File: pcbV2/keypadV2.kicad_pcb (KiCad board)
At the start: 2 copper layers, 93.7 x 93.3 mm, 79 parts, among them J1 Conn_01x02_Female, J2 USB_C_Receptacle, J3 Conn_01x03_Male, Q1 Q_NMOS_GSD, SW1 SW_Push, SW10 SW_Push, SW11 SW_Push, SW12 SW_Push, SW13 SW_SPDT, SW14 SW_Push, SW15 SW_Push, SW16 SW_Push, SW17 SW_DIP_x03, SW2 SW_Push, SW3 SW_Push, SW4 SW_Push, SW5 SW_Push, SW6 SW_Push, SW7 SW_Push, SW8 SW_Push, SW9 SW_Push, U1 Teensy4.0, U2 Waveshare_OLED_RGB

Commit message: component layout v1
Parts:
- added J6: Conn_01x03_Male, Connector_PinSocket_2.54mm:PinSocket_1x03_P2.54mm_Vertical, B.Cu at (160.8, 119.1)
- C13, C14, C15, D13, D26, D27, D28, D29, J3, R1, SW13: moved to B.Cu
- Q1, R2, R3, R4: moved to F.Cu
- moved C14 174.5 mm to (101.3, 162.8), turned to 180 degrees
- moved D28 167.5 mm to (141.1, 167.3), turned to 180 degrees
- moved C13 165.0 mm to (100.1, 123.2), turned to 180 degrees
- moved D26 157.1 mm to (99.2, 127.8), turned to 180 degrees
- moved D27 141.6 mm to (101.3, 167.4), turned to 180 degrees
- moved C16 132.2 mm to (138.2, 127.8), turned to 90 degrees
- moved C15 128.8 mm to (141.0, 162.8), turned to 180 degrees
- moved D29 117.1 mm to (143.4, 127.8)
- moved R5 112.6 mm to (223.5, 98.3)
- moved D13 108.1 mm to (149.4, 107.4), turned to 90 degrees
- moved R1 81.0 mm to (146.6, 107.4), turned to 270 degrees
- moved C2 69.6 mm to (213.1, 113.2), turned to 90 degrees
- moved C7 67.7 mm to (229.0, 102.6)
- moved C11 67.7 mm to (230.0, 112.5)
- moved C4 67.7 mm to (230.0, 109.2)
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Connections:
- D29 pad 4: Net-(D22-Pad2) -> RGB_UNDER
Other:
- outline, holes or cut-outs redrawn
- net class Safe_Min added: clearance 0.135, trace_width 0.135, via_dia 0.55, via_drill 0.3
- rule trace_min: 0.2 -> 0.135

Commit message: Start daughterboard
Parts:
- moved SW17 3.78 mm to (129.0, 124.0)
- moved SW14 3.57 mm to (136.4, 124.7), turned to 0 degrees
- moved J1 2.29 mm to (131.3, 115.1), turned to 90 degrees
- moved D29 0.38 mm to (143.8, 127.8)
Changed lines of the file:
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@@
     (46 B.CrtYd user)
     (47 F.CrtYd user)
-    (48 B.Fab user hide)
+    (48 B.Fab user)
     (49 F.Fab user)
   )
@@
   )
   (module LED_SMD:LED_WS2812B_PLCC4_5.0x5.0mm_P3.2mm (layer B.Cu)
-    (at 143.383 127.762)
+    (at 143.764 127.762)
     (descr https://cdn-shop.adafruit.com/datasheets/WS2812B.pdf)
     (tags "LED RGB NeoPixel")
@@
   )
   (module Connector_PinHeader_2.00mm:PinHeader_1x02_P2.00mm_Vertical (layer B.Cu)
-    (at 129.413 113.792 270)
+    (at 131.318 115.062 90)
     (descr "Through hole straight pin header, 1x02, 2.00mm pitch, single row")
     (tags "Through hole pin header THT 1x02 2.00mm single row")
@@
       (effects (font (size 1 1) (thickness 0.15)) (justify mirror))
     )
-    (pad 1 thru_hole rect (at 0 0 270) (size 1.35 1.35) (drill 0.8) (layers *.Cu *.Mask)
+    (pad 1 thru_hole rect (at 0 0 90) (size 1.35 1.35) (drill 0.8) (layers *.Cu *.Mask)
       (net 37 USB_DATA+))
-    (pad 2 thru_hole oval (at 0 -2 270) (size 1.35 1.35) (drill 0.8) (layers *.Cu *.Mask)
+    (pad 2 thru_hole oval (at 0 -2 90) (size 1.35 1.35) (drill 0.8) (layers *.Cu *.Mask)
       (net 38 USB_DATA-))
     (model ${KISYS3DMOD}/Connector_PinHeader_2.00mm.3dshapes/PinHeader_1x02_P2.00mm_Vertical.wrl
@@
   )
   (module custom:BTN_B3S-1000P (layer B.Cu)
-    (at 136.0805 121.158 90)
-    (attr smd)
-    (fp_text reference SW14 (at -4.4 0 180) (layer B.SilkS)
-      (effects (font (size 1 1) (thickness 0.15)) (justify mirror))
-    )
-    (fp_text value SW_Push (at 0 0 90) (layer B.Fab)
+    (at 136.398 124.714)
+    (attr smd)
+    (fp_text reference SW14 (at -4.4 0 270) (layer B.SilkS)
+      (effects (font (size 1 1) (thickness 0.15)) (justify mirror))
+    )
+    (fp_text value SW_Push (at 0 0) (layer B.Fab)
       (effects (font (size 1 1) (thickness 0.15)) (justify mirror))
     )
@@
     (fp_line (start 3.15 -5) (end -3.15 -5) (layer B.CrtYd) (width 0.05))
     (fp_line (start -3.15 -5) (end -3.15 5) (layer B.CrtYd) (width 0.05))
-    (pad 4 smd rect (at -2.25 3.975 90) (size 1.3 1.55) (layers B.Cu B.Paste B.Mask))
-    (pad 1 smd rect (at -2.25 -3.975 90) (size 1.3 1.55) (layers B.Cu B.Paste B.Mask)
+    (pad 4 smd rect (at -2.25 3.975) (size 1.3 1.55) (layers B.Cu B.Paste B.Mask))
+    (pad 1 smd rect (at -2.25 -3.975) (size 1.3 1.55) (layers B.Cu B.Paste B.Mask)
       (net 54 ON_OFF))
-    (pad 3 smd rect (at 2.25 3.975 90) (size 1.3 1.55) (layers B.Cu B.Paste B.Mask))
-    (pad 2 smd rect (at 2.25 -3.975 90) (size 1.3 1.55) (layers B.Cu B.Paste B.Mask)
+    (pad 3 smd rect (at 2.25 3.975) (size 1.3 1.55) (layers B.Cu B.Paste B.Mask))
+    (pad 2 smd rect (at 2.25 -3.975) (size 1.3 1.55) (layers B.Cu B.Paste B.Mask)
       (net 1 GND))
   )
@@
   )
   (module custom:DIP3_219-3MSTR (layer B.Cu)
-    (at 126.238 121.412 180)
+    (at 129.032 123.952 180)
     (attr smd)
     (fp_text reference SW17 (at -4.605 0 270) (layer B.SilkS)

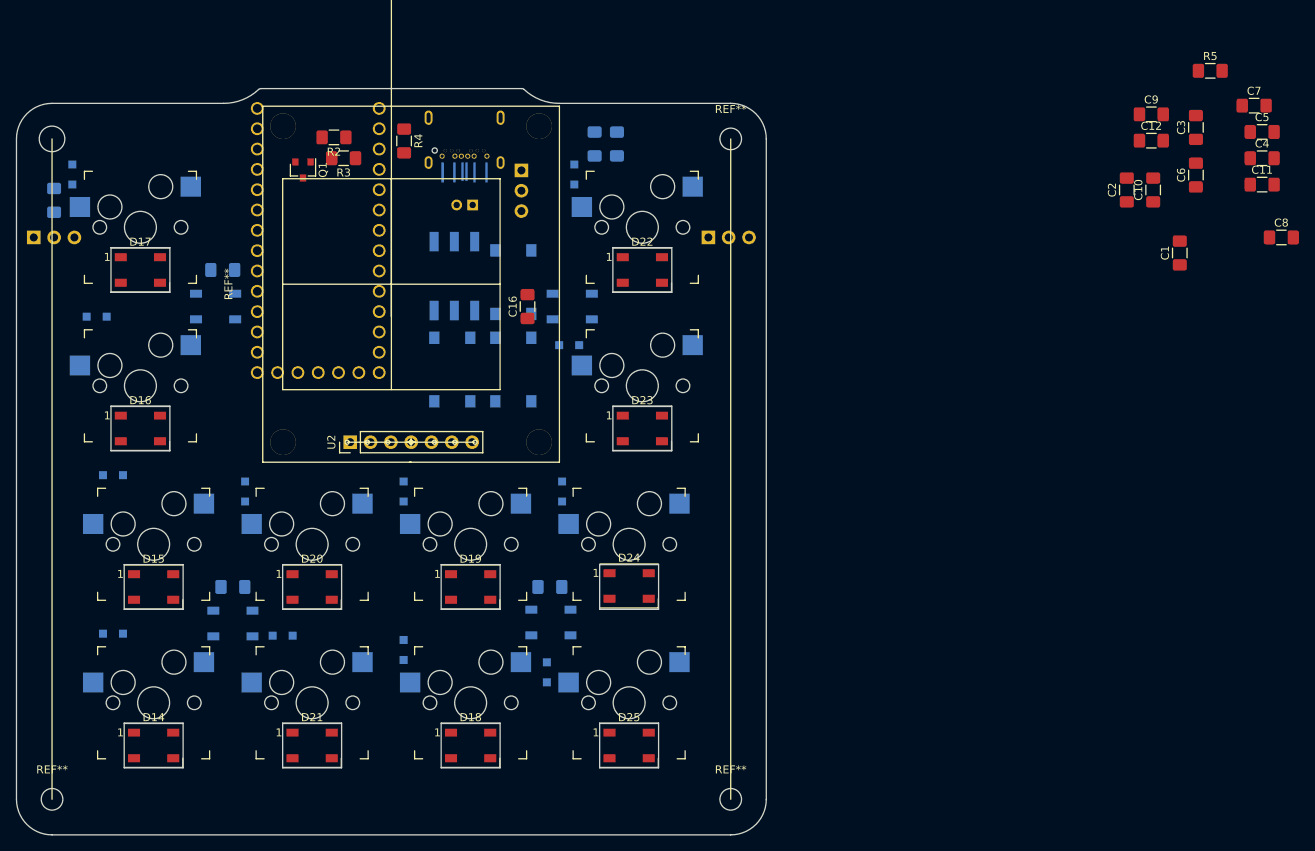
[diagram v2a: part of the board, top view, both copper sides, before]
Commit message: Updated schematic on mainboard, LEDs moved to daughter board
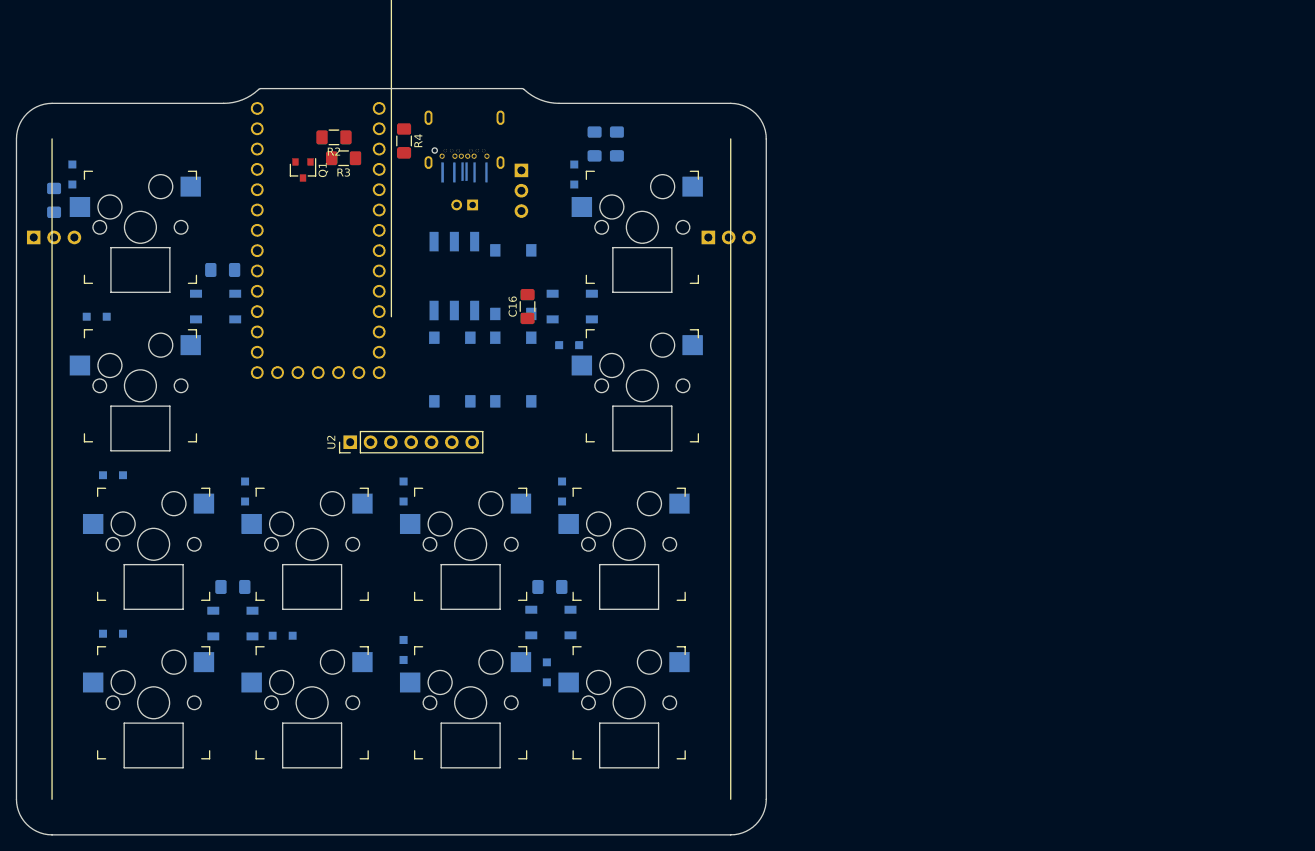
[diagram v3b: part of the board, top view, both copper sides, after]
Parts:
- removed C1, C10, C11, C12, C2, C3, C4, C5, C6, C7, C8, C9: 1000uF, Capacitor_SMD:C_1206_3216Metric_Pad1.42x1.75mm_HandSolder
- removed D14, D15, D16, D17, D18, D19, D20, D21, D22, D23, D24, D25: WS2812B, LED_SMD:LED_WS2812B_PLCC4_5.0x5.0mm_P3.2mm
- removed R5: R_DIN, Resistor_SMD:R_1206_3216Metric_Pad1.42x1.75mm_HandSolder
- removed REF** (x3): MountingHole_2.7mm_M2.5, MountingHole:MountingHole_2.7mm_M2.5
- removed REF**: MountingHole_3.2mm_M3, MountingHole:MountingHole_3.2mm_M3
- removed REF**: Waveshare_LCD_mount V2, custom:Waveshare_LCD_mount V2

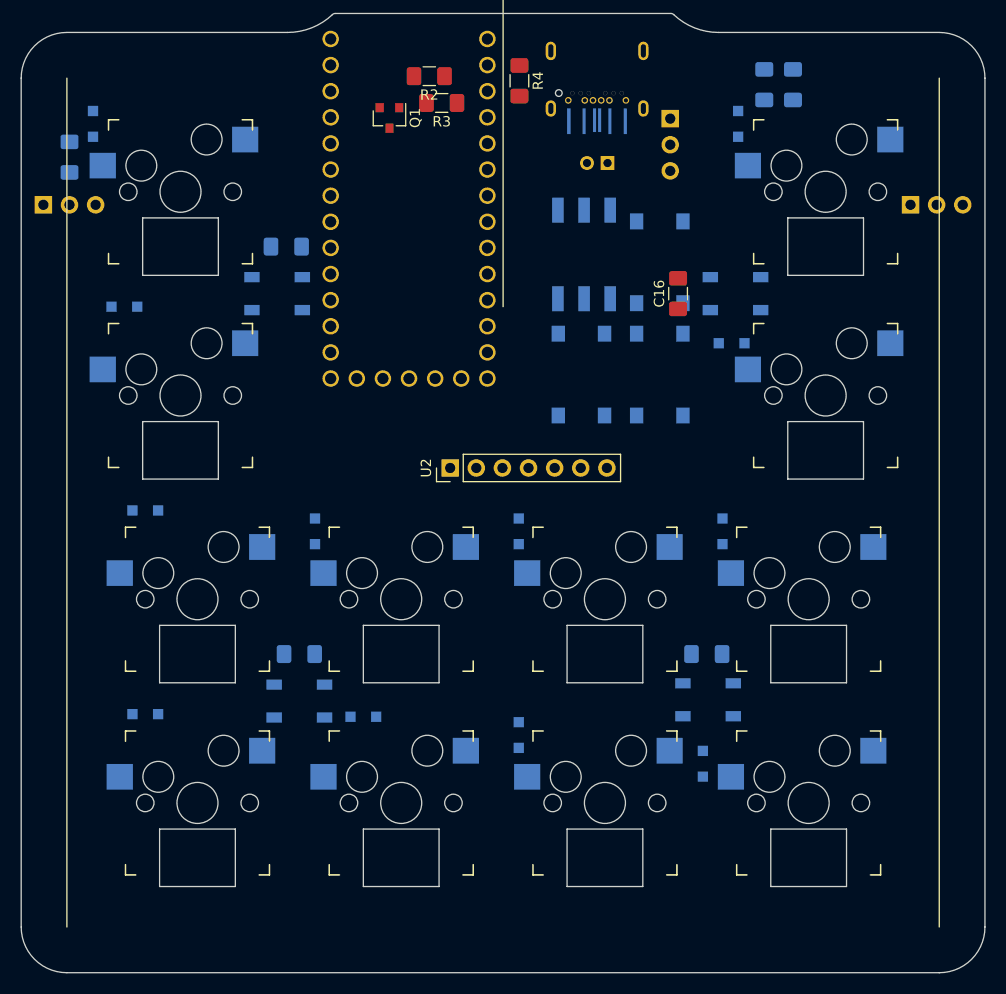
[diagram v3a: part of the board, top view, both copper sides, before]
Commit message: added mouting holes
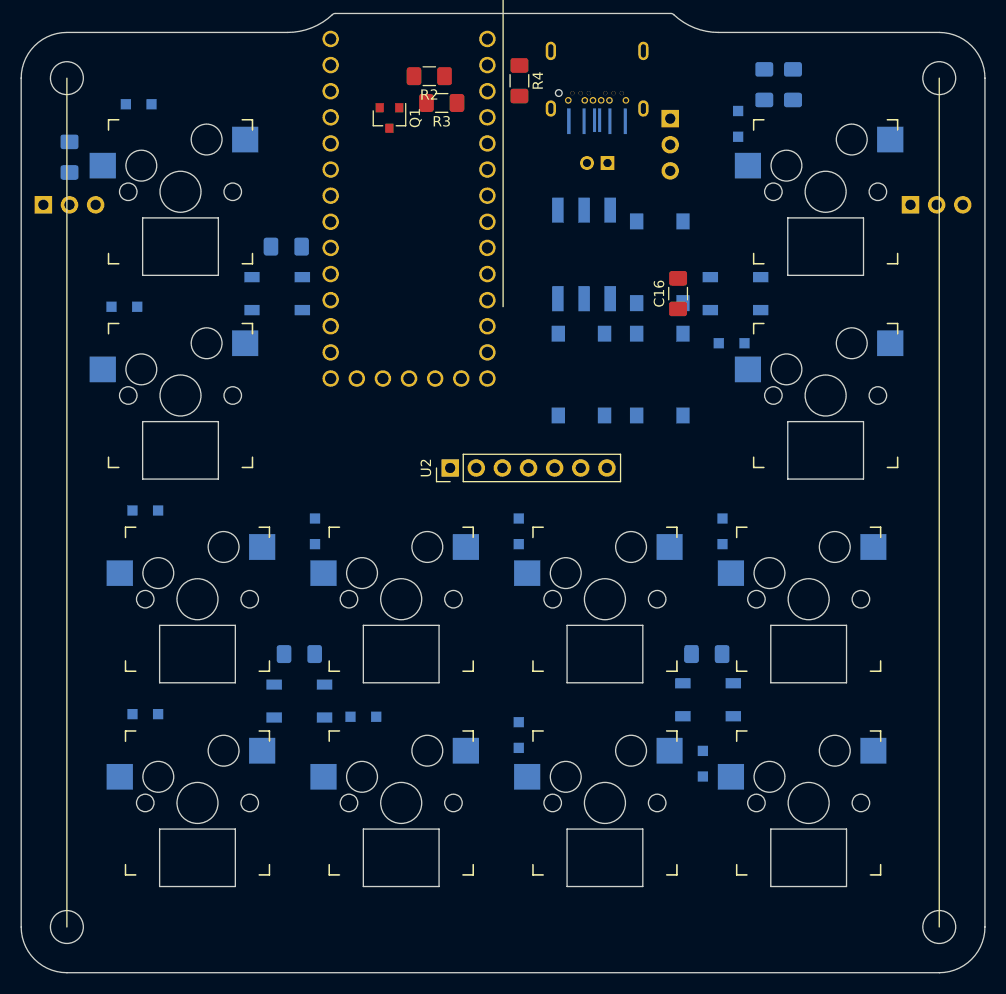
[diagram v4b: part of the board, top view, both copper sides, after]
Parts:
- added H1: MountingHole, MountingHole:MountingHole_3.2mm_M3, F.Cu at (78.7, 106.8)
- added H2: MountingHole, MountingHole:MountingHole_3.2mm_M3, F.Cu at (78.7, 189.4)
- added H3: MountingHole, MountingHole:MountingHole_3.2mm_M3, F.Cu at (163.6, 189.4)
- added H4: MountingHole, MountingHole:MountingHole_3.2mm_M3, F.Cu at (163.6, 106.8)
- moved D1 4.84 mm to (85.7, 109.3), turned to 180 degrees

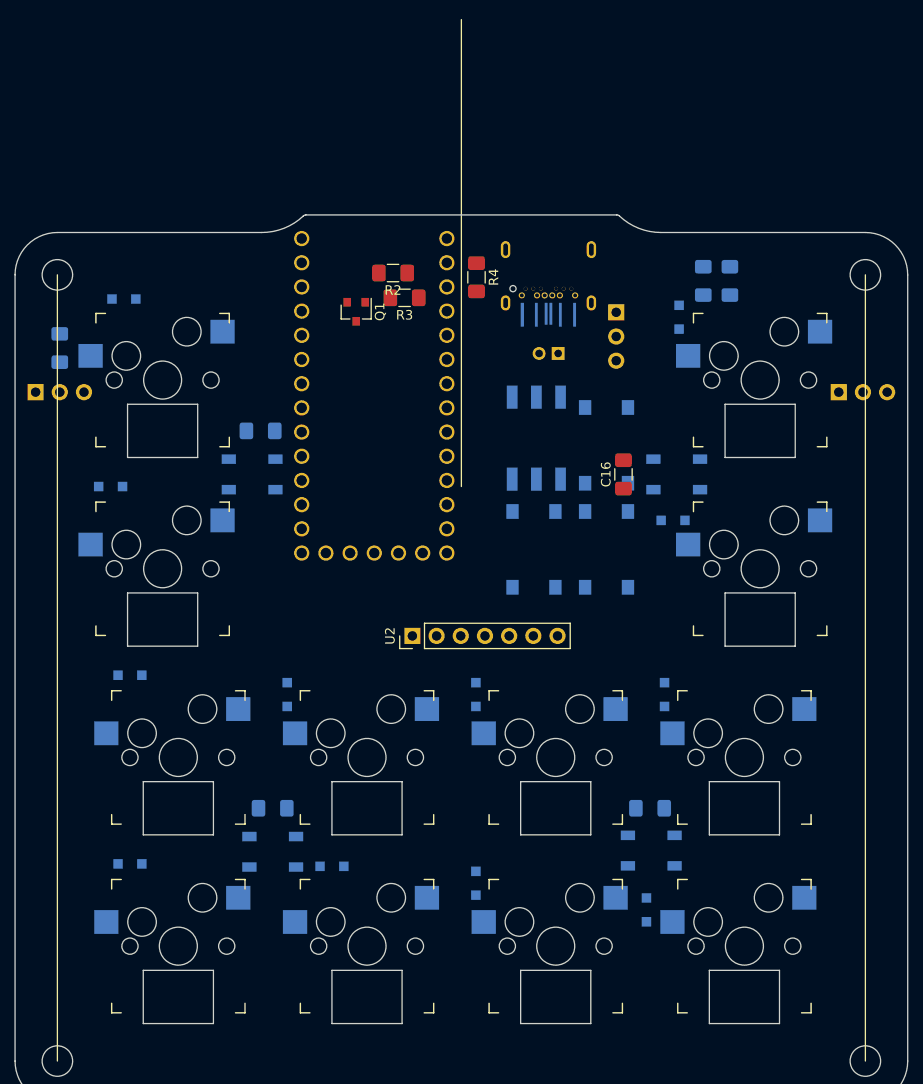
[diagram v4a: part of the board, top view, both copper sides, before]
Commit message: Added components for 2nd RGB Data line
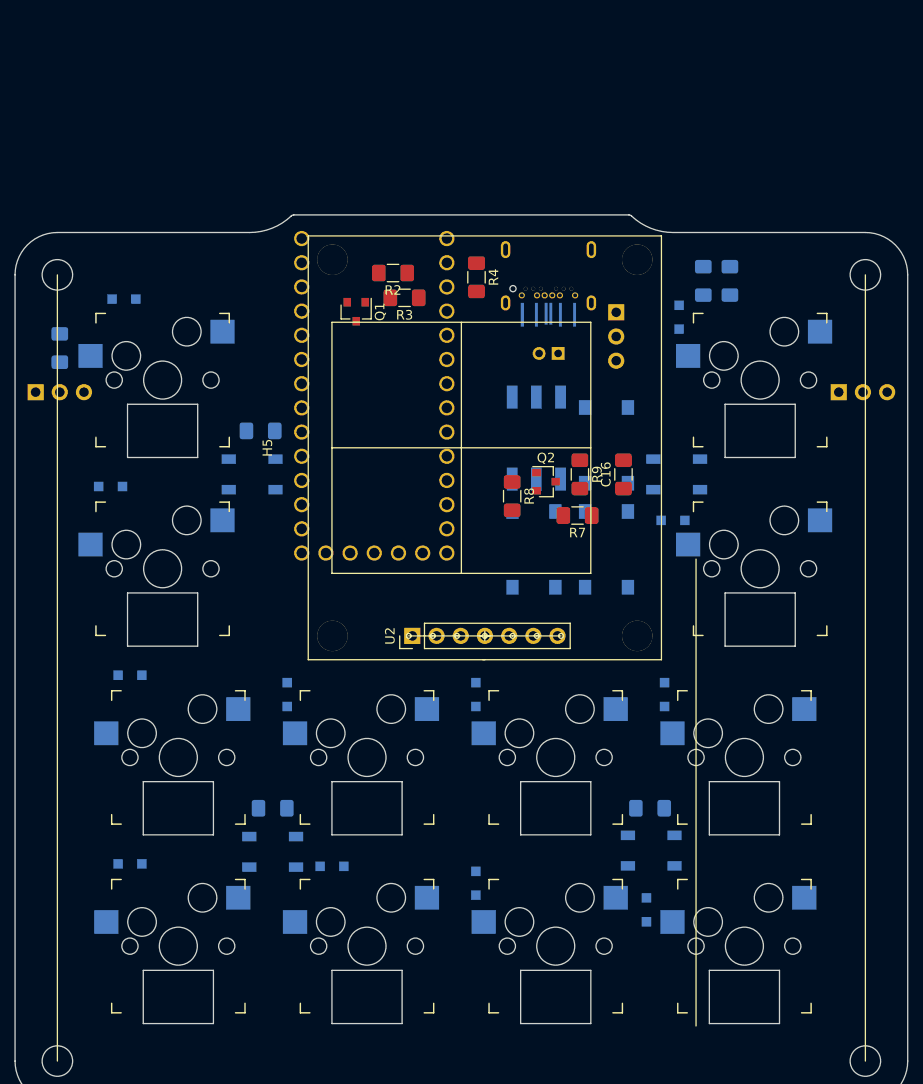
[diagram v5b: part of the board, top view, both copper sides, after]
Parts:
- added H5: Display Mount, custom:Waveshare_LCD_mount V2, F.Cu at (121.2, 125.0)
- added Q2: Q_NMOS_GSD, Package_TO_SOT_SMD:SOT-23, F.Cu at (130.0, 128.5)
- added R7: JUMPER, Resistor_SMD:R_1206_3216Metric_Pad1.42x1.75mm_HandSolder, F.Cu at (133.3, 132.1)
- added R8: 10K, Resistor_SMD:R_1206_3216Metric_Pad1.42x1.75mm_HandSolder, F.Cu at (126.5, 130.0)
- added R9: 10K, Resistor_SMD:R_1206_3216Metric_Pad1.42x1.75mm_HandSolder, F.Cu at (133.6, 127.8)
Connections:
- net RGB_DATA renamed RGB_DATA1
- J6 pad 2: RGB_UNDER -> Net-(J6-Pad2)
- U1 pad 21: BTN -> RGB_DATA2
- U1 pad 25: Net-(U1-Pad25) -> BTN
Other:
- outline, holes or cut-outs redrawn
